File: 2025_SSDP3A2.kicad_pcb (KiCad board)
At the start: 4 copper layers, 58.4 x 28.8 mm, 66 parts, among them J1 SolderPad, J2 SolderPad, J3 SolderPad, J4 SolderPad, Q1 CSD19534Q5A, Q2 BSC0805LS, U1 LM5146RGYR

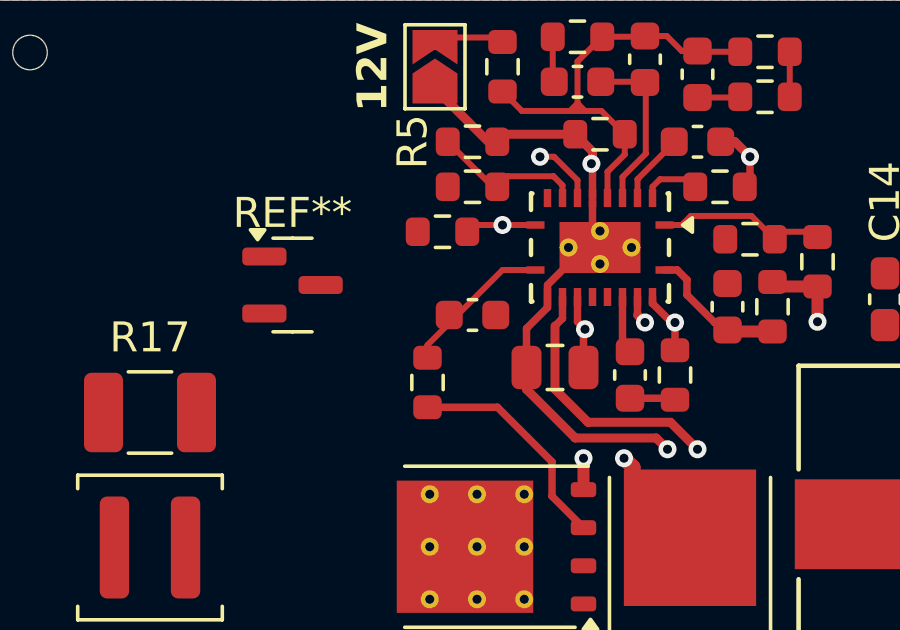
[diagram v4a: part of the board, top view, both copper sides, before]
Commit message: Updated ILIM values
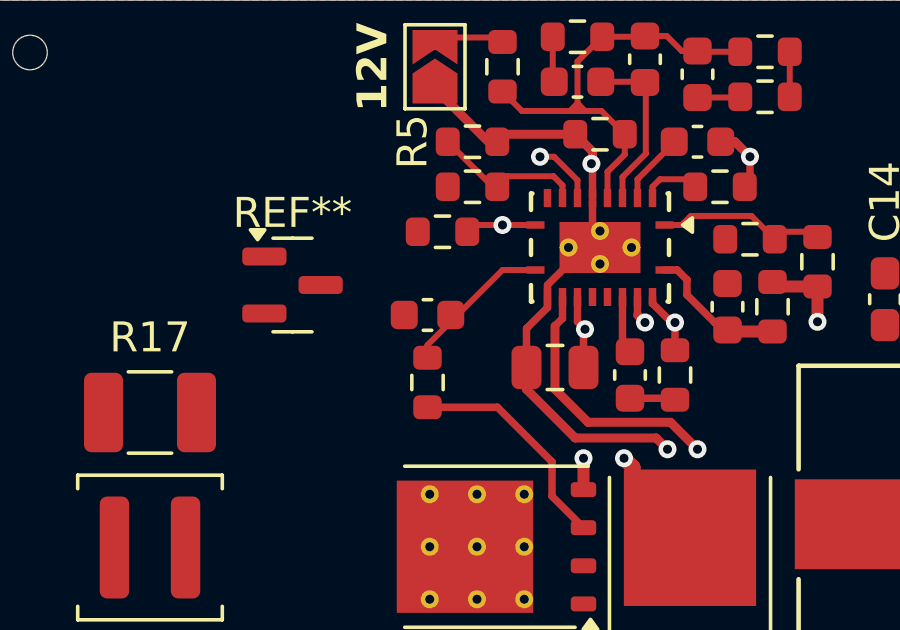
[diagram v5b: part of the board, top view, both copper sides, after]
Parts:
- moved C11 1.50 mm to (141.2, 110.5), turned to 180 degrees
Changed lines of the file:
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@@
 	(footprint "Capacitor_SMD:C_0603_1608Metric"
 		(layer "F.Cu")
-		(at 142.75 110.5)
+		(at 141.25 110.5 180)
 		(descr "Capacitor SMD 0603 (1608 Metric), square (rectangular) end terminal, IPC_7351 nominal, (Body size source: IPC-SM-782 page 76, https://www.pcb-3d.com/wordpress/wp-content/uploads/ipc-sm-782a_amendment_1_and_2.pdf), generated with kicad-footprint-generator")
 		(tags "capacitor")
@@
 		)
 		(property "Datasheet" "~"
-			(at 0 0 0)
+			(at 0 0 180)
 			(unlocked yes)
 			(layer "F.Fab")
@@
 		)
 		(property "Description" "GCM1885C2A180JA16D"
-			(at 0 0 0)
+			(at 0 0 180)
 			(unlocked yes)
 			(layer "F.Fab")
@@
 		)
 		(property "LCSC PN" "C913624"
-			(at 0 0 0)
+			(at 0 0 180)
 			(unlocked yes)
 			(layer "F.Fab")
@@
 		)
 		(property "Part Type" "Extended"
-			(at 0 0 0)
+			(at 0 0 180)
 			(unlocked yes)
 			(layer "F.Fab")
@@
 		)
 		(property "FT Rotation Offset" "0"
-			(at 0 0 0)
+			(at 0 0 180)
 			(unlocked yes)
 			(layer "F.Fab")
@@
 		)
 		(property "LCSC ALT1" ""
-			(at 0 0 0)
+			(at 0 0 180)
 			(unlocked yes)
 			(layer "F.Fab")
@@
 		)
 		(property "PART ALT1" ""
-			(at 0 0 0)
+			(at 0 0 180)
 			(unlocked yes)
 			(layer "F.Fab")
@@
 		)
 		(property "ESR" ""
-			(at 0 0 0)
+			(at 0 0 180)
 			(unlocked yes)
 			(layer "F.Fab")
@@
 		)
 		(property "MANUFACTURER" "Murata Electronics"
-			(at 0 0 0)
+			(at 0 0 180)
 			(unlocked yes)
 			(layer "F.Fab")
@@
 		)
 		(property "MAXIMUM_PACKAGE_HEIGHT" ""
-			(at 0 0 0)
+			(at 0 0 180)
 			(unlocked yes)
 			(layer "F.Fab")
@@
 		)
 		(property "Package" ""
-			(at 0 0 0)
+			(at 0 0 180)
 			(unlocked yes)
 			(layer "F.Fab")
@@
 		)
 		(property "Power" ""
-			(at 0 0 0)
+			(at 0 0 180)
 			(unlocked yes)
 			(layer "F.Fab")
@@
 		)
 		(property "STANDARD" ""
-			(at 0 0 0)
+			(at 0 0 180)
 			(unlocked yes)
 			(layer "F.Fab")
@@
 		)
 		(property "Voltage" "100V"
-			(at 0 0 0)
+			(at 0 0 180)
 			(unlocked yes)
 			(layer "F.Fab")
@@
 		)
 		(property "Tolerance" "5%"
-			(at 0 0 0)
+			(at 0 0 180)
 			(unlocked yes)
 			(layer "F.Fab")
@@
 		(attr smd)
 		(fp_line
+			(start -0.14058 0.51)
+			(end 0.14058 0.51)
+			(stroke
+				(width 0.12)
+				(type solid)
+			)
+			(layer "F.SilkS")
+		)
+		(fp_line
 			(start -0.14058 -0.51)
 			(end 0.14058 -0.51)
@@
 		)
 		(fp_line
-			(start -0.14058 0.51)
-			(end 0.14058 0.51)
-			(stroke
-				(width 0.12)
-				(type solid)
-			)
-			(layer "F.SilkS")
+			(start 1.48 0.73)
+			(end -1.48 0.73)
+			(stroke
+				(width 0.05)
+				(type solid)
+			)
+			(layer "F.CrtYd")
+		)
+		(fp_line
+			(start 1.48 -0.73)
+			(end 1.48 0.73)
+			(stroke
+				(width 0.05)
+				(type solid)
+			)
+			(layer "F.CrtYd")
+		)
+		(fp_line
+			(start -1.48 0.73)
+			(end -1.48 -0.73)
+			(stroke
+				(width 0.05)
+				(type solid)
+			)
+			(layer "F.CrtYd")
 		)
 		(fp_line
@@
 		)
 		(fp_line
-			(start -1.48 0.73)
-			(end -1.48 -0.73)
-			(stroke
-				(width 0.05)
-				(type solid)
-			)
-			(layer "F.CrtYd")
-		)
-		(fp_line
-			(start 1.48 -0.73)
-			(end 1.48 0.73)
-			(stroke
-				(width 0.05)
-				(type solid)
-			)
-			(layer "F.CrtYd")
-		)
-		(fp_line
-			(start 1.48 0.73)
-			(end -1.48 0.73)
-			(stroke
-				(width 0.05)
-				(type solid)
-			)
-			(layer "F.CrtYd")
+			(start 0.8 0.4)
+			(end -0.8 0.4)
+			(stroke
+				(width 0.1)
+				(type solid)
+			)
+			(layer "F.Fab")
+		)
+		(fp_line
+			(start 0.8 -0.4)
+			(end 0.8 0.4)
+			(stroke
+				(width 0.1)
+				(type solid)
+			)
+			(layer "F.Fab")
+		)
+		(fp_line
+			(start -0.8 0.4)
+			(end -0.8 -0.4)
+			(stroke
+				(width 0.1)
+				(type solid)
+			)
+			(layer "F.Fab")
 		)
 		(fp_line
@@
 			(layer "F.Fab")
 		)
-		(fp_line
-			(start -0.8 0.4)
-			(end -0.8 -0.4)
-			(stroke
-				(width 0.1)
-				(type solid)
-			)
-			(layer "F.Fab")
-		)
-		(fp_line
-			(start 0.8 -0.4)
-			(end 0.8 0.4)
-			(stroke
-				(width 0.1)
-				(type solid)
-			)
-			(layer "F.Fab")
-		)
-		(fp_line
-			(start 0.8 0.4)
-			(end -0.8 0.4)
-			(stroke
-				(width 0.1)
-				(type solid)
-			)
-			(layer "F.Fab")
-		)
 		(fp_text user "${REFERENCE}"
 			(at 0 0 0)
@@
 		)
 		(pad "1" smd roundrect
-			(at -0.775 0)
+			(at -0.775 0 180)
 			(size 0.9 0.95)
 			(layers "F.Cu" "F.Mask" "F.Paste")
@@
 		)
 		(pad "2" smd roundrect
-			(at 0.775 0)
+			(at 0.775 0 180)
 			(size 0.9 0.95)
 			(layers "F.Cu" "F.Mask" "F.Paste")

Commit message: Something changed
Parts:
- removed REF**: SOT-23, Package_TO_SOT_SMD:SOT-23
- moved D1 20.1 mm to (132.8, 107.0), turned to 0 degrees
- moved C1 0.34 mm to (146.2, 122.8)
- moved C2 0.25 mm to (137.2, 123.5)
- moved C3 0.25 mm to (140.5, 123.5)
- moved C4 0.25 mm to (143.8, 123.5)
- moved C5 0.25 mm to (134.0, 123.5)
- moved C6 0.25 mm to (130.5, 123.5)

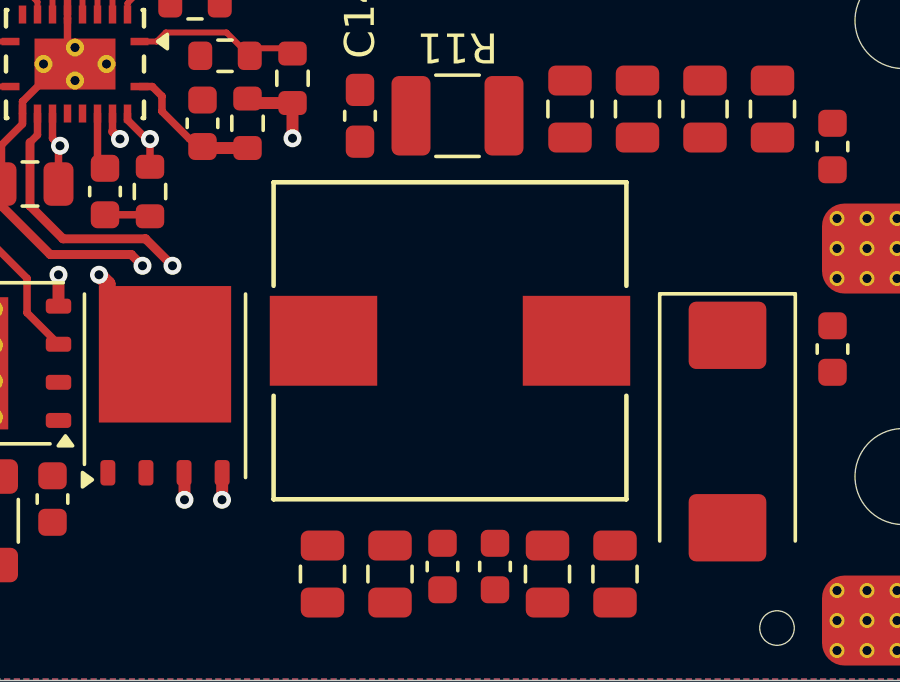
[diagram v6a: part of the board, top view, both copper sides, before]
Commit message: Revised simulations, revised compensation network
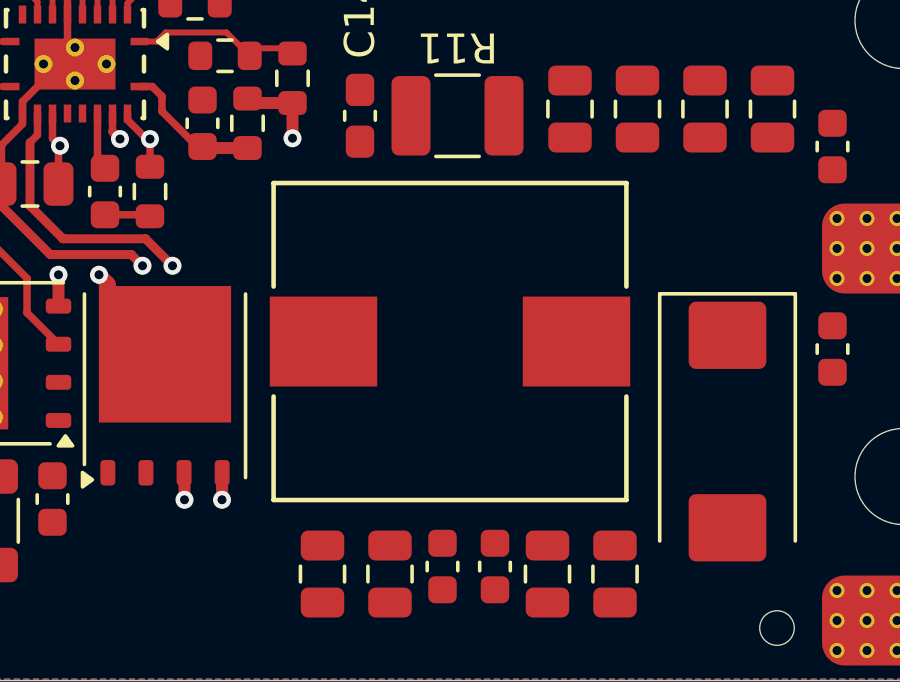
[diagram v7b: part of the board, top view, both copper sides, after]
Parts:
- C13: value 100pF -> 47pF
- R10: value 10k -> 12k
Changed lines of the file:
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@@
 			)
 		)
-		(property "Datasheet" "https://www.infineon.com/part/BSC0805LS"
+		(property "Datasheet" "https://www.infineon.com/assets/row/public/documents/24/49/infineon-bsc0805ls-datasheet-en.pdf"
 			(at 0 0 90)
 			(unlocked yes)
@@
 			)
 		)
-		(property "Value" "100pF"
+		(property "Value" "47pF"
 			(at 0 1.43 90)
 			(layer "F.Fab")
@@
 			)
 		)
-		(property "Description" "CL10C101JB8NNNC"
+		(property "Description" "CL10C470JB8NNNC"
 			(at 0 0 270)
 			(unlocked yes)
@@
 			)
 		)
-		(property "LCSC PN" "C14858"
+		(property "LCSC PN" "C1671"
 			(at 0 0 270)
 			(unlocked yes)
@@
 	(footprint "PA4342-472NLT:IND_PA4342_PUL-M"
 		(layer "F.Cu")
-		(at 159.5 117.475)
+		(at 159.5 117.5)
 		(tags "PA4342.472NLT ")
 		(property "Reference" "L2"
@@
 			)
 		)
-		(property "Value" "10k"
+		(property "Value" "12k"
 			(at 0 1.43 0)
 			(layer "F.Fab")
@@
 			)
 		)
-		(property "Description" "0603WAF1002T5E"
+		(property "Description" "0603WAF1202T5E"
 			(at 0 0 180)
 			(unlocked yes)
@@
 			)
 		)
-		(property "LCSC PN" "C25804"
+		(property "LCSC PN" "C22790"
 			(at 0 0 180)
 			(unlocked yes)
@@
 			)
 		)
-		(property "Description" "Resistor, US symbol"
+		(property "Description" "1206W4F100JT5E"
 			(at 0 0 180)
 			(unlocked yes)
@@
 			)
 		)
+		(property "FT Rotation Offset" "0"
+			(at 0 0 180)
+			(unlocked yes)
+			(layer "F.Fab")
+			(hide yes)
+			(effects
+				(font
+					(size 1 1)
+					(thickness 0.15)
+				)
+			)
+		)
+		(property "LCSC PN" "C17903"
+			(at 0 0 180)
+			(unlocked yes)
+			(layer "F.Fab")
+			(hide yes)
+			(effects
+				(font
+					(size 1 1)
+					(thickness 0.15)
+				)
+			)
+		)
+		(property "MANUFACTURER" "UNI-ROYAL"
+			(at 0 0 180)
+			(unlocked yes)
+			(layer "F.Fab")
+			(hide yes)
+			(effects
+				(font
+					(size 1 1)
+					(thickness 0.15)
+				)
+			)
+		)
+		(property "Part Type" "Basic"
+			(at 0 0 180)
+			(unlocked yes)
+			(layer "F.Fab")
+			(hide yes)
+			(effects
+				(font
+					(size 1 1)
+					(thickness 0.15)
+				)
+			)
+		)
+		(property "Power" "0.25W"
+			(at 0 0 180)
+			(unlocked yes)
+			(layer "F.Fab")
+			(hide yes)
+			(effects
+				(font
+					(size 1 1)
+					(thickness 0.15)
+				)
+			)
+		)
+		(property "Tolerance" "1%"
+			(at 0 0 180)
+			(unlocked yes)
+			(layer "F.Fab")
+			(hide yes)
+			(effects
+				(font
+					(size 1 1)
+					(thickness 0.15)
+				)
+			)
+		)
 		(property ki_fp_filters "R_*")
 		(sheetname "/")
@@
 	)
 	(segment
-		(start 149.725001 107.499999)
-		(end 150.026 107.199)
+		(start 150.026 107.199)
+		(end 152.049 107.199)
 		(width 0.2)
 		(layer "F.Cu")
@@
 	)
 	(segment
-		(start 152.049 107.199)
-		(end 152.825 107.975)
+		(start 149.150001 107.499999)
+		(end 149.725001 107.499999)
 		(width 0.2)
 		(layer "F.Cu")
@@
 	)
 	(segment
-		(start 149.150001 107.499999)
-		(end 149.725001 107.499999)
+		(start 149.725001 107.499999)
+		(end 150.026 107.199)
 		(width 0.2)
 		(layer "F.Cu")
@@
 	)
 	(segment
-		(start 153.925 107.725)
-		(end 154 107.65)
+		(start 152.049 107.199)
+		(end 152.825 107.975)
 		(width 0.2)
 		(layer "F.Cu")
@@
 	)
 	(segment
-		(start 152.575 107.725)
-		(end 153.925 107.725)
+		(start 153.925 107.725)
+		(end 154 107.65)
 		(width 0.2)
 		(layer "F.Cu")
@@
 	)
 	(segment
-		(start 150.026 107.199)
-		(end 152.049 107.199)
+		(start 152.575 107.725)
+		(end 153.925 107.725)
 		(width 0.2)
 		(layer "F.Cu")

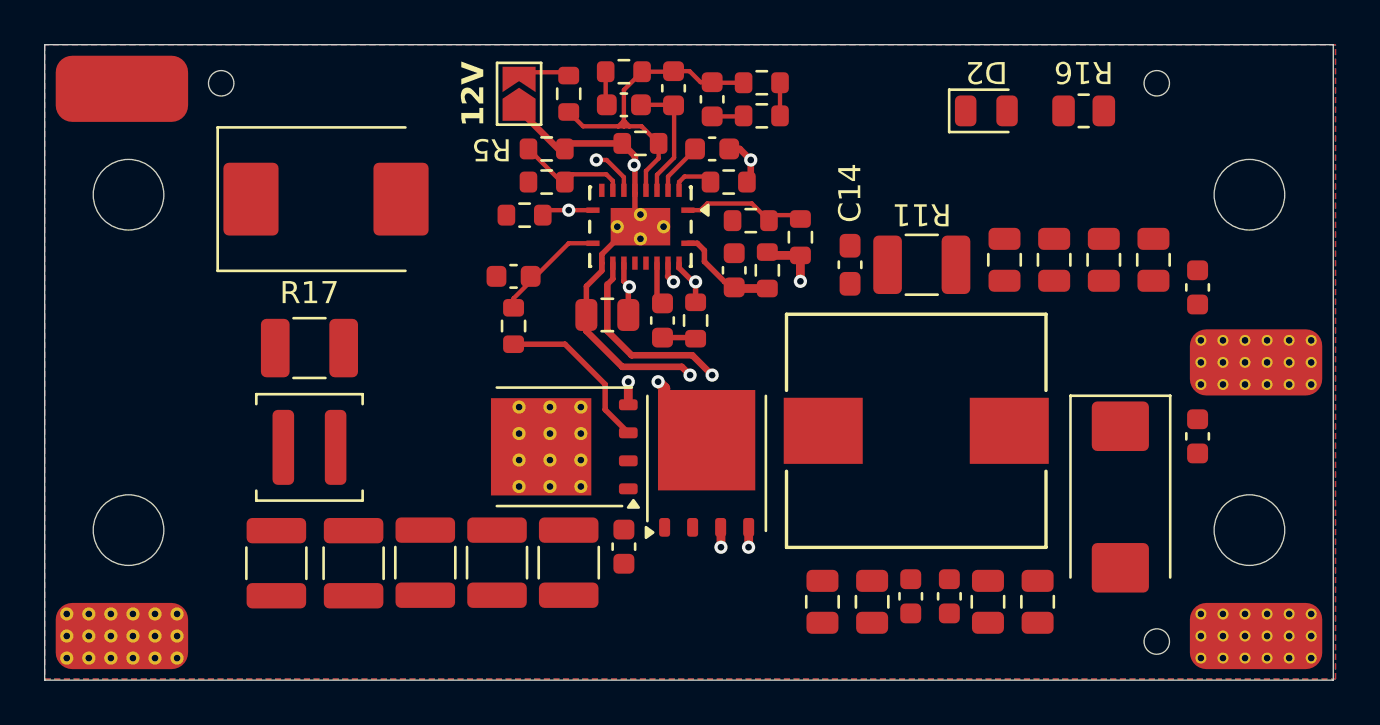
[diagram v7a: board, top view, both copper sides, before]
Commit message: Changed output capacitors for better layout
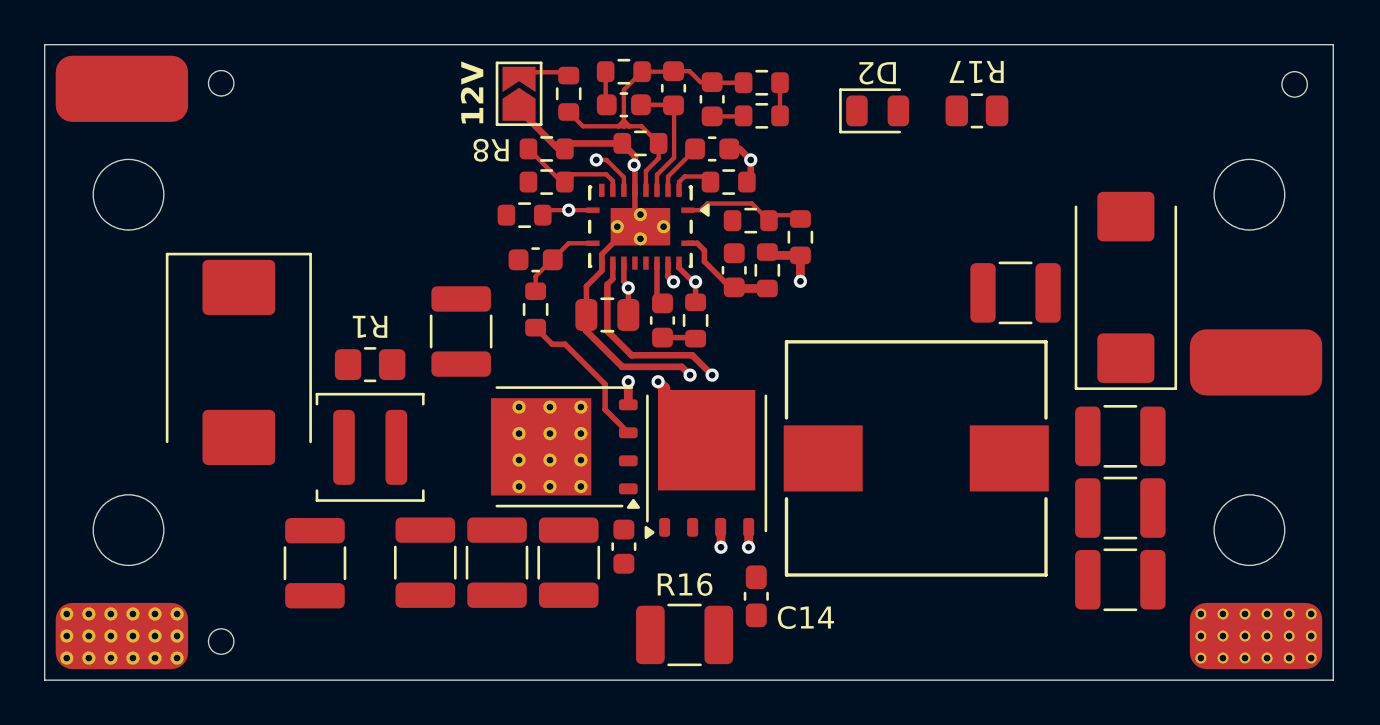
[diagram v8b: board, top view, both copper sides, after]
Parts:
- removed the C20 at (162.8, 125.2)
- removed C21, C22, C23, C24, C25: 22uF, Capacitor_SMD:C_0805_2012Metric
- removed C26, C27: 100nF, Capacitor_SMD:C_0603_1608Metric
- added REF**: Symbol_HighVoltage_Triangle_6x6mm_Copper, Symbol:Symbol_HighVoltage_Triangle_6x6mm_Copper, B.Cu at (124.0, 114.4)
- C16, C17: value 100nF -> 22uF; footprint Capacitor_SMD:C_0603_1608Metric -> Capacitor_SMD:C_1210_3225Metric
- C18, C19: footprint Capacitor_SMD:C_0805_2012Metric -> Capacitor_SMD:C_1210_3225Metric
- R1: renamed from R17; footprint Resistor_SMD:R_1210_3225Metric_Pad1.30x2.65mm_HandSolder -> Resistor_SMD:R_0805_2012Metric_Pad1.20x1.40mm_HandSolder
- moved H7 42.4 mm to (128.0, 127.0)
- moved R16 19.9 mm to (149.0, 126.8), turned to 180 degrees
- moved C14 15.6 mm to (152.2, 125.0), turned to -90 degrees
- moved C19 15.4 mm to (164.0, 111.2), turned to 180 degrees
- moved C18 13.5 mm to (168.8, 124.2), turned to 0 degrees
- moved C16 12.0 mm to (168.8, 117.8), turned to 0 degrees
- moved C5 11.6 mm to (138.9, 113.0), turned to 90 degrees
- moved C20 9.50 mm to (169.0, 111.0), turned to 90 degrees
- moved C17 8.72 mm to (168.8, 121.0), turned to 0 degrees
- moved D1 8.39 mm to (128.8, 114.4), turned to -90 degrees
- moved H5 6.25 mm to (176.7, 101.8)
- moved D2 4.93 mm to (157.8, 103.0)
- moved R17 4.84 mm to (162.2, 103.0), turned to 180 degrees
- moved R1 2.85 mm to (134.8, 114.5)
- moved L1 2.75 mm to (134.8, 118.2)
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- renumbered C15 to C10, C12 to C11, C13 to C12, C10 to C13, C11 to C15, C28 to C20, C9 to C7, C7 to C8, C8 to C9, R14 to R10, R10 to R11, R13 to R12, R15 to R13, R9 to R14, R8 to R15, R11 to R16, R16 to R17, R6 to R2, R2 to R3, R3 to R4, R7 to R5, R4 to R6, R1 to R7, R5 to R8, R12 to R9
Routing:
- net /ILIM: track 5.06 -> 3.90 mm
- net /SW: track 18.1 -> 17.5 mm
- removed copper zone on B.Cu, net PGND
- removed copper zone on F.Cu, net PGND
- removed copper zone on In1.Cu, net PGND
- removed copper zone on In2.Cu, net PGND
